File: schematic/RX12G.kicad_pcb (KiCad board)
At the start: 2 copper layers, 43 parts, among them J1 ICSP, J2 TSW-104-08-G-T-RA, J3 TSW-104-08-G-T-RA, J4 TSW-104-08-G-T-RA, J5 Conn_01x03, J6 Conn_01x03, J7 USB_B_Micro, J8 Conn_01x03, Q1 2N7002P_215, SW1 SW_MEC_5E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

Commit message: Initial pcb layout - footprints only
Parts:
- moved J6 102.3 mm to (139.5, 124.2)
- moved C9 101.6 mm to (116.0, 105.3), turned to -90 degrees
- moved D4 101.6 mm to (147.3, 124.3), turned to -90 degrees
- moved C10 100.6 mm to (122.9, 111.4), turned to 180 degrees
- moved R5 100.2 mm to (145.7, 124.3), turned to -90 degrees
- moved R11 99.7 mm to (127.4, 113.7), turned to 90 degrees
- moved U3 99.6 mm to (112.6, 105.2), turned to 180 degrees
- moved R8 99.5 mm to (118.0, 116.3)
- moved R3 98.3 mm to (117.4, 99.7), turned to 90 degrees
- moved C8 96.8 mm to (111.6, 108.8)
- moved R10 96.7 mm to (125.6, 113.6), turned to 90 degrees
- moved D1 92.3 mm to (111.5, 99.6), turned to 90 degrees
- moved U2 89.1 mm to (124.5, 108.8), turned to 180 degrees
- moved D2 83.0 mm to (115.5, 99.7), turned to 90 degrees
- moved C11 83.0 mm to (124.9, 106.2), turned to 180 degrees
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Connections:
- J2 pad 1: CH9_SBUS4 -> CH12_SBUS1
- J2 pad 10: CH12_SBUS1 -> CH9_SBUS4
- J2 pad 4: CH10_SBUS3 -> CH11_SBUS2
- J2 pad 7: CH11_SBUS2 -> CH10_SBUS3
- J3 pad 1: CH5 -> CH8
- J3 pad 10: CH8 -> CH5
- J3 pad 4: CH6 -> CH7
- J3 pad 7: CH7 -> CH6
- J4 pad 1: CH1 -> CH4
- J4 pad 10: CH4 -> CH1
- J4 pad 4: CH2 -> CH3
- J4 pad 7: CH3 -> CH2
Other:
- board outline added: 50 x 37.4 mm

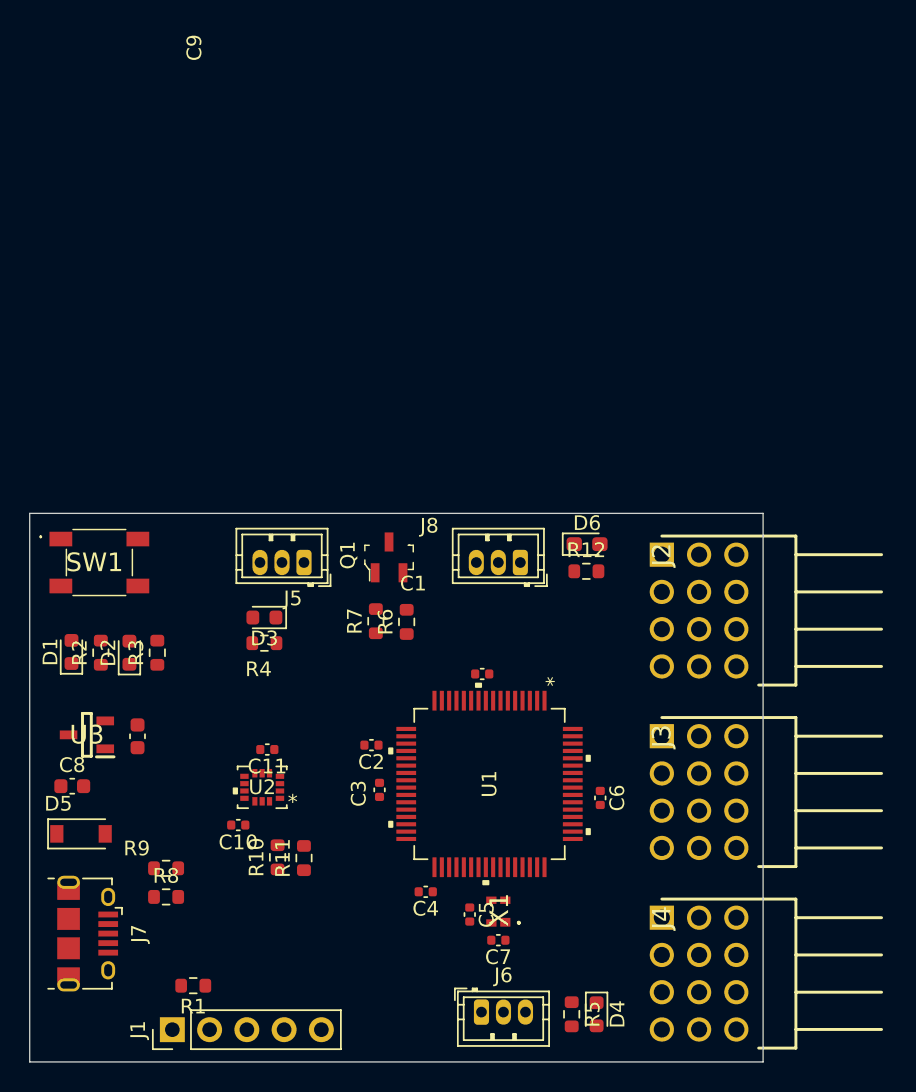
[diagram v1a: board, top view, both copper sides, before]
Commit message: Workable pcb layout
Needs work on silkscreen
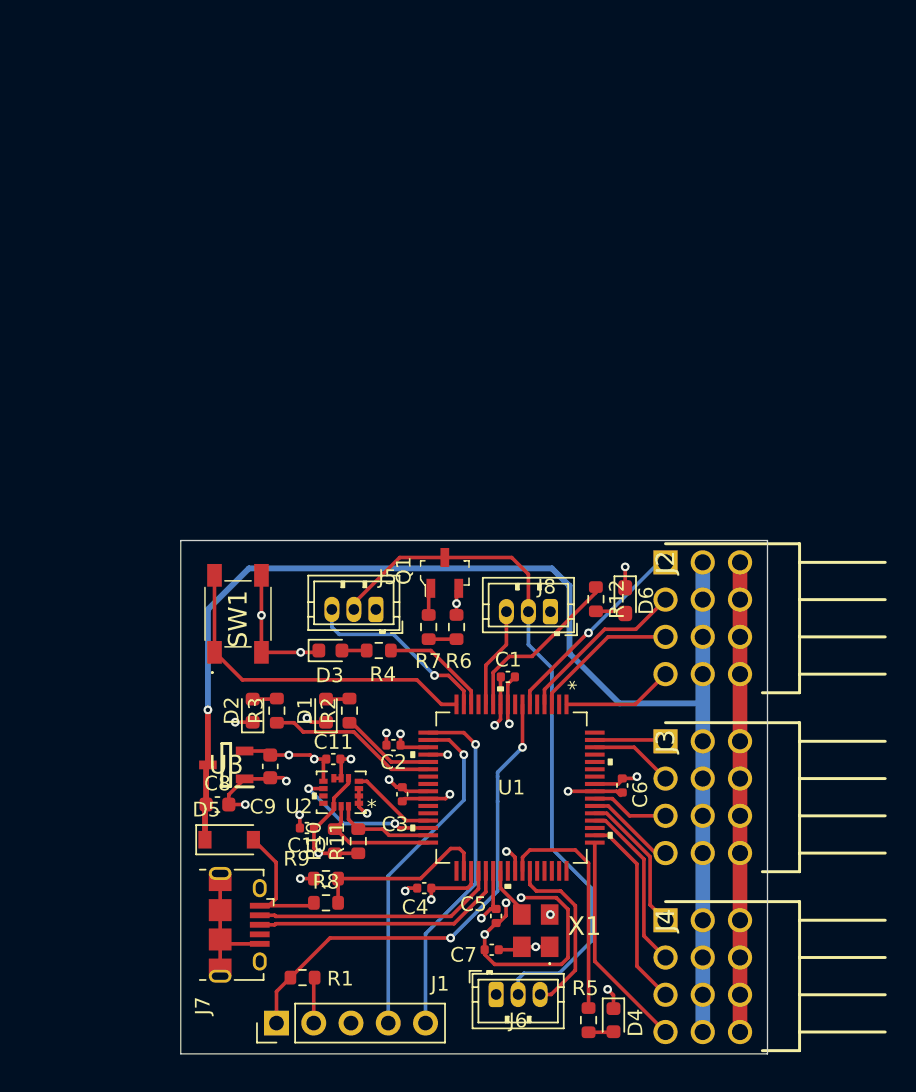
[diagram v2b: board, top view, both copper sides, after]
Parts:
- X1: footprint SamacSys Parts:AMPMAFB120000T -> SamacSys Parts:ASTMUPCE3312000MHZLJET
- moved D1 17.8 mm to (128.9, 103.6)
- moved R2 17.4 mm to (130.5, 103.6)
- moved R9 10.9 mm to (128.9, 115.0)
- moved R8 10.9 mm to (128.9, 116.7)
- moved J7 10.4 mm to (123.0, 118.2)
- moved D5 10.1 mm to (122.3, 112.4)
- moved SW1 10.1 mm to (122.9, 97.0), turned to 90 degrees
- moved C8 9.98 mm to (121.5, 110.0)
- moved U3 9.72 mm to (122.1, 107.3)
- moved D2 9.28 mm to (123.9, 103.6)
- moved C9 9.28 mm to (125.1, 107.4)
- moved R3 9.06 mm to (125.5, 103.6)
- moved R4 7.82 mm to (132.5, 99.5)
- moved R1 7.47 mm to (127.3, 121.8)
- moved J1 7.11 mm to (125.5, 124.9)
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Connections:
- U1 pad 29: IMU_INT2 -> IMU_INT1
- U1 pad 30: IMU_INT1 -> IMU_INT2
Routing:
- net GND: track 0.00 -> 102.1 mm, vias 0 -> 24
- net Vin: track 0.00 -> 89.2 mm, vias 0 -> 1
- net Net-(J5-Pad2): track 0.00 -> 48.0 mm
- net +3V3: track 0.00 -> 44.1 mm, vias 0 -> 10
- net MCLR: track 0.00 -> 33.5 mm, vias 0 -> 2
- net PGC: track 0.00 -> 24.0 mm, vias 0 -> 1
- net PGD: track 0.00 -> 23.3 mm, vias 0 -> 1
- net Bind_Button: track 0.00 -> 23.2 mm
- net D+: track 0.00 -> 17.8 mm
- net D-: track 0.00 -> 16.9 mm
- net LED_SAT2: track 0.00 -> 15.9 mm
- net CH1: track 0.00 -> 14.9 mm
- net CH12_SBUS1: track 0.00 -> 13.8 mm, vias 0 -> 1
- net CH2: track 0.00 -> 13.4 mm
- net SAT1_RX: track 0.00 -> 12.9 mm, vias 0 -> 1
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- added copper zone on In2.Cu, net +3V3
- added copper zone on In1.Cu, net GND
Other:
- board size 50 x 37.4 mm -> 40 x 35 mm
- copper layers 2 -> 4

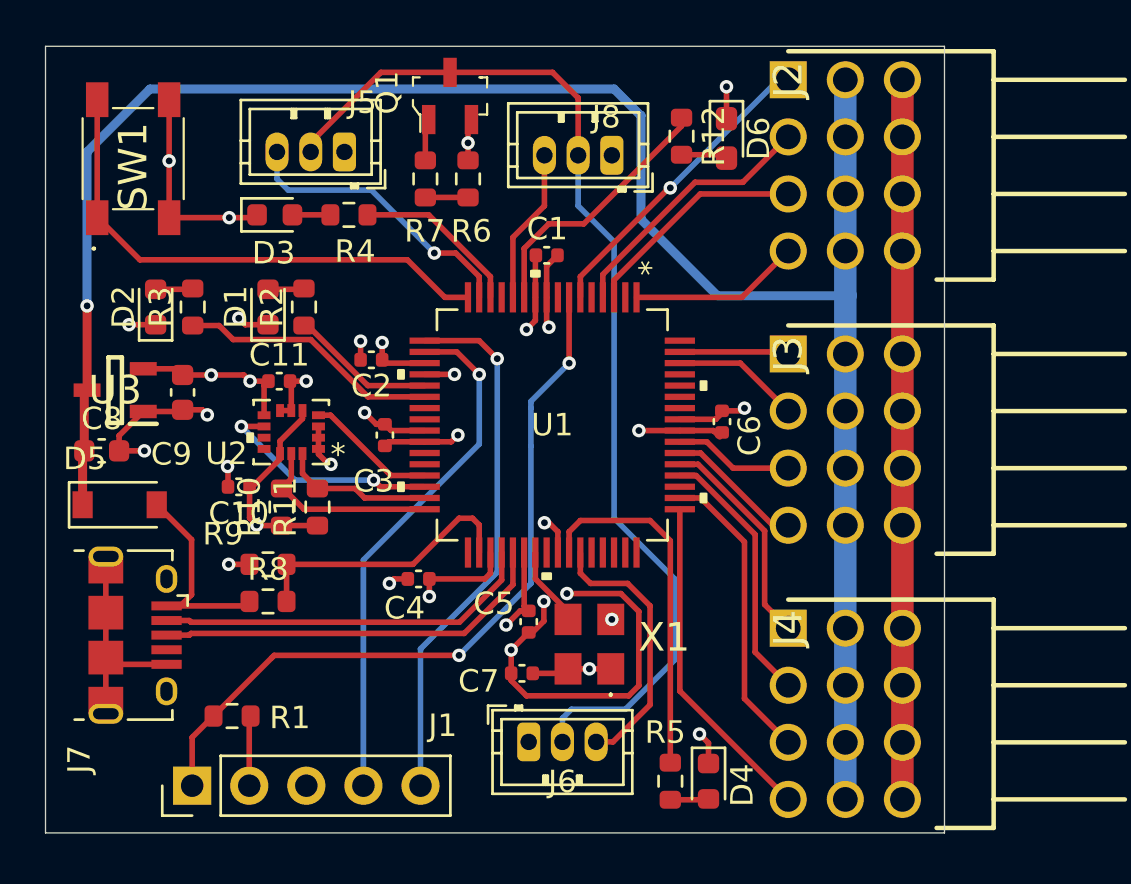
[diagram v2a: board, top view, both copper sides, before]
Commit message: Improved board ouline
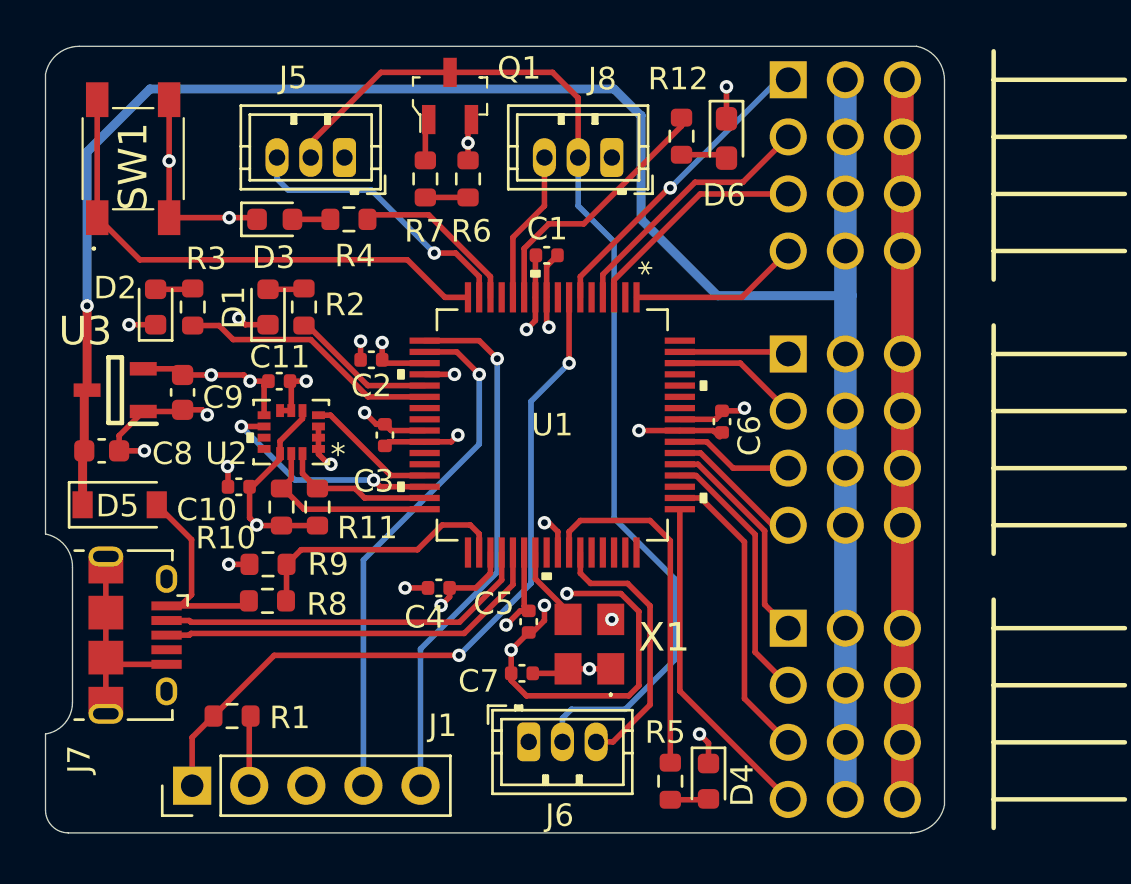
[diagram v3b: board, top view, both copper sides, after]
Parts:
- moved C4 0.98 mm to (136.5, 116.1)
- moved J5 0.25 mm to (132.3, 97.0)
- moved D3 0.20 mm to (129.2, 99.7)
- moved R4 0.20 mm to (132.5, 99.7)
- moved J8 0.10 mm to (144.2, 97.0)
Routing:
- net Net-(D5-Pad2): track 9.74 -> 9.12 mm
- net +3V3: track 44.1 -> 43.5 mm
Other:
- outline, holes or cut-outs redrawn

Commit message: Generated BOM, added gerber settings
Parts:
- moved C7 6.36 mm to (146.5, 119.0), turned to 90 degrees
- moved D4 5.71 mm to (142.9, 123.6)
- moved J6 4.09 mm to (136.5, 122.1)
- moved J1 3.31 mm to (122.2, 124.7)
- moved R5 2.46 mm to (144.6, 123.6)
- moved X1 0.76 mm to (143.9, 118.3)
- moved R1 0.32 mm to (127.6, 121.9)
- moved C5 0.28 mm to (140.3, 117.4)
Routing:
- net GND: track 101.8 -> 113.2 mm
- net LED_SAT2: track 15.9 -> 20.3 mm
- net Net-(J5-Pad2): track 48.0 -> 44.4 mm
- net MCLR: track 33.5 -> 36.3 mm
- net +3V3: track 43.5 -> 46.0 mm
- net PGD: track 23.3 -> 24.5 mm
- net PGC: track 24.0 -> 25.0 mm
- net SAT2_RX: track 12.1 -> 12.2 mm, vias 0 -> 2
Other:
- board text added: "- + S"
- board text added: "1"
- board text added: "12"
- board text added: "JLCJLCJLCJLC"
- board text added: "RX12G"
- board text added: "V1.0 QES 2022"

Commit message: Fixed missing  SAT_POWER connection
Also re-assigned some pins to improve pcb layout
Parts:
- moved C10 5.46 mm to (130.2, 106.8)
- moved C11 1.40 mm to (128.0, 106.8)
- moved C4 0.30 mm to (136.8, 116.1)
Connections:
- U1 pad 13: unconnected-(U1-Pad13) -> SAT_POWER
- U1 pad 40: unconnected-(U1-Pad40) -> SAT2_RX
- U1 pad 42: LED_SAT2 -> unconnected-(U1-Pad42)
- U1 pad 43: SAT2_RX -> unconnected-(U1-Pad43)
- U1 pad 46: unconnected-(U1-Pad46) -> LED_SAT2
- U1 pad 47: unconnected-(U1-Pad47) -> GND
- U1 pad 48: unconnected-(U1-Pad48) -> GND
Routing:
- net SAT_POWER: track 1.90 -> 6.97 mm
- net LED_SAT2: track 20.3 -> 16.5 mm
- net GND: track 113.2 -> 115.4 mm, vias 24 -> 23
- net +3V3: track 46.0 -> 44.4 mm, vias 10 -> 11
- net Net-(D5-Pad2): track 9.12 -> 10.4 mm
- net SAT2_RX: track 12.2 -> 11.5 mm, vias 2 -> 1
